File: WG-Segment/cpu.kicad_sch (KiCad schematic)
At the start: 28 parts, among them J201 Conn_01x03, J202 Conn_01x02, J203 Conn_01x04, SW201 SPST-NO, U201 W25Q16JV, U202 RP2040, Y201 12MHz

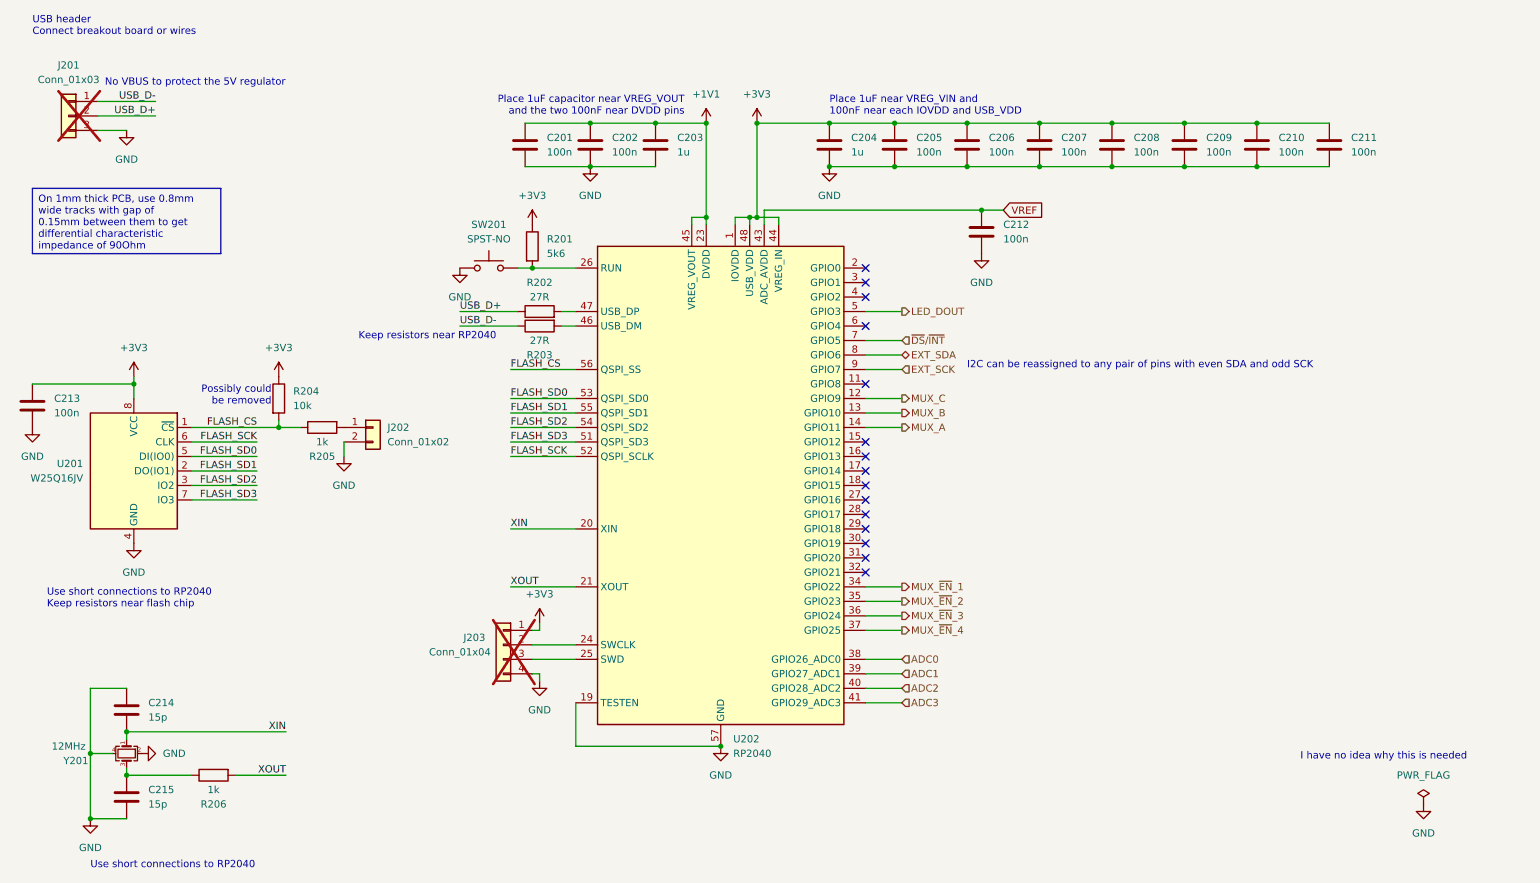
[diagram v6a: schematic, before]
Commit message: Minor pinout adjustments
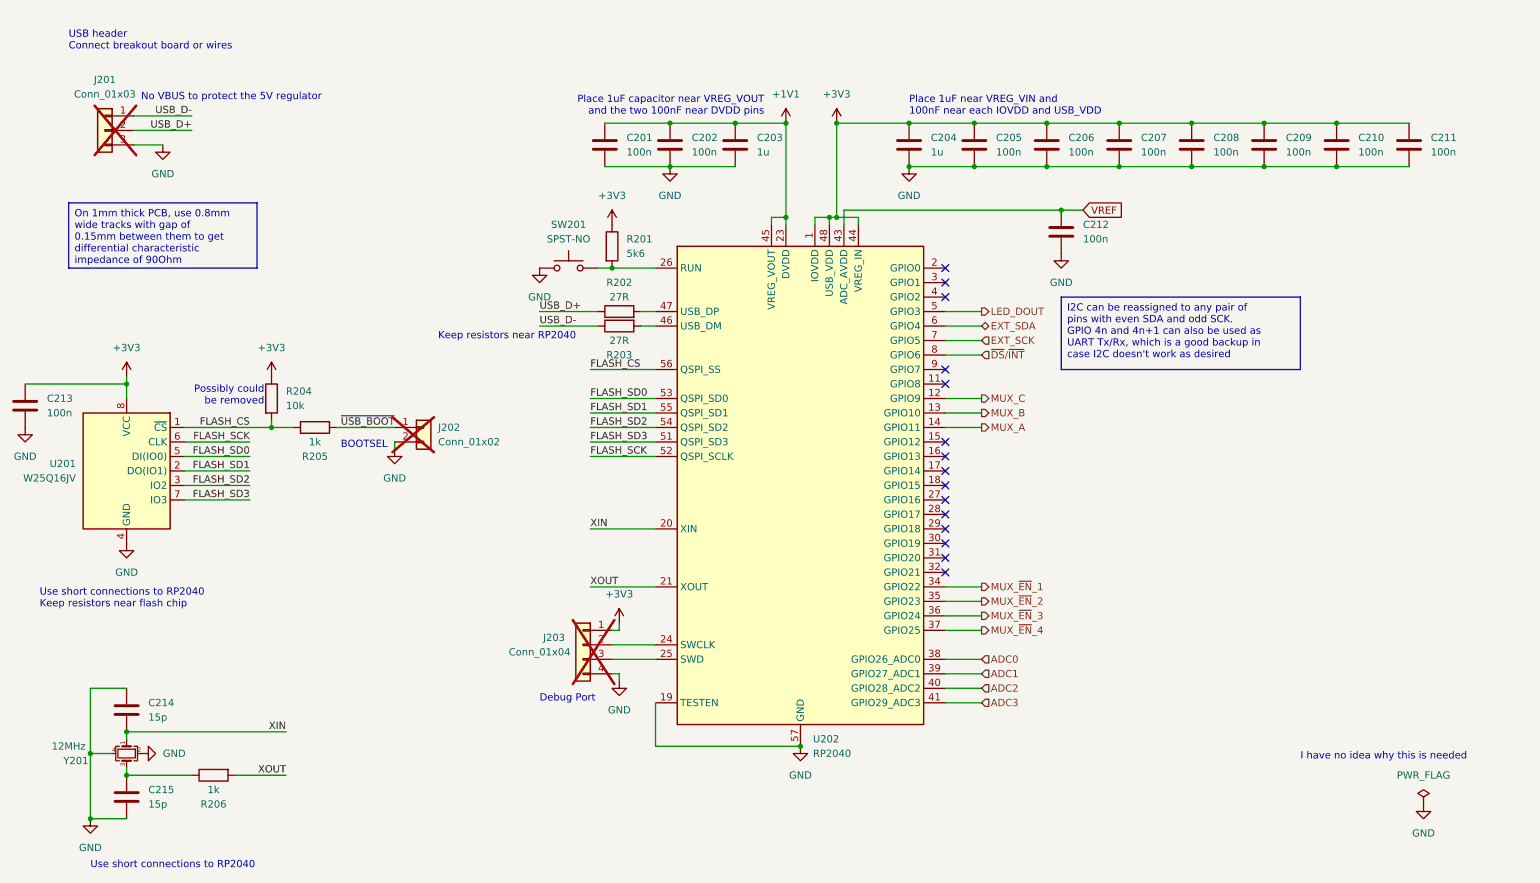
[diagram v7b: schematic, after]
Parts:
- J202: now not fitted; now left out of the parts list
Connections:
- net EXT_SCK: now also U202.7 (GPIO5); no longer U202.9 (GPIO7)
- net EXT_SDA: now also U202.6 (GPIO4); no longer U202.8 (GPIO6)
- net ~{DS}/~{INT}: now also U202.8 (GPIO6); no longer U202.7 (GPIO5)
- net ~{USB_BOOT}: now reaches J202.1 (Pin_1), R205.2
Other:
- note added: "BOOTSEL"
- note added: "Debug Port"
- note removed: "I2C can be reassigned to any pair of pins with even SDA and odd SCK"
- moved on the sheet: C201, C202, C203, C204, C205, C206, C207, C208, C209, C210, C211, C212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

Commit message: Fix build issues
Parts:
- C201, C202, C205, C206, C207, C208, C209, C210, C211, C212, C213: value 100n -> 0.1u; Desc (none) -> CAP CER 0.1uF 10V 0402
- C203, C204: Desc (none) -> CAP CER 1uF 10V 0402
- C214, C215: Desc (none) -> CAP CER 15pF 10V 0402
- R201: Desc (none) -> RES 5k6 1/16W 1% 0402
- R202, R203: Desc (none) -> RES 27R 1/16W 1% 0402
- R204: Desc (none) -> RES 10k 1/16W 1% 0402
- R205, R206: Desc (none) -> RES 1k 1/16W 1% 0402
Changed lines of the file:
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@@
       (effects (font (size 1.27 1.27)) (justify left))
     )
-    (property "Value" "100n" (at 270.51 40.64 0)
+    (property "Value" "0.1u" (at 270.51 40.64 0)
       (effects (font (size 1.27 1.27)) (justify left))
     )
@@
       (effects (font (size 1.27 1.27)) hide)
     )
-    (property "Description" "CAP CER 100nF 10V 0402" (at 266.7 39.37 0)
+    (property "Desc" "CAP CER 0.1uF 10V 0402" (at 266.7 39.37 0)
       (effects (font (size 1.27 1.27)) hide)
     )
@@
       (effects (font (size 1.27 1.27)) hide)
     )
-    (property "Description" "CAP CER 15pF 10V 0402" (at 41.91 138.43 0)
+    (property "Desc" "CAP CER 15pF 10V 0402" (at 41.91 138.43 0)
       (effects (font (size 1.27 1.27)) hide)
     )
@@
       (effects (font (size 1.27 1.27)) hide)
     )
-    (property "Description" "" (at 38.1 36.83 0)
-      (effects (font (size 1.27 1.27)) hide)
-    )
     (pin "1")
     (pin "3")
@@
       (effects (font (size 1.27 1.27)) hide)
     )
-    (property "Description" "" (at 119.38 60.96 0)
-      (effects (font (size 1.27 1.27)) hide)
-    )
     (pin "2")
     (pin "1")
@@
       (effects (font (size 1.27 1.27)) hide)
     )
-    (property "Description" "RES 10k 1/16W 1% 0402" (at 67.31 83.82 0)
+    (property "Desc" "RES 10k 1/16W 1% 0402" (at 67.31 83.82 0)
       (effects (font (size 1.27 1.27)) hide)
     )
@@
       (effects (font (size 1.27 1.27)) hide)
     )
-    (property "Description" "" (at 93.98 88.9 0)
-      (effects (font (size 1.27 1.27)) hide)
-    )
     (pin "2")
     (pin "1")
@@
       (effects (font (size 1.27 1.27)) hide)
     )
-    (property "Description" "RES 27R 1/16W 1% 0402" (at 128.27 71.12 0)
+    (property "Desc" "RES 27R 1/16W 1% 0402" (at 128.27 71.12 0)
       (effects (font (size 1.27 1.27)) hide)
     )
@@
       (effects (font (size 1.27 1.27)) hide)
     )
-    (property "Description" "CAP CER 15pF 10V 0402" (at 41.91 153.67 0)
+    (property "Desc" "CAP CER 15pF 10V 0402" (at 41.91 153.67 0)
       (effects (font (size 1.27 1.27)) hide)
     )
@@
       (effects (font (size 1.27 1.27)) (justify left))
     )
-    (property "Value" "100n" (at 257.81 40.64 0)
+    (property "Value" "0.1u" (at 257.81 40.64 0)
       (effects (font (size 1.27 1.27)) (justify left))
     )
@@
       (effects (font (size 1.27 1.27)) hide)
     )
-    (property "Description" "CAP CER 100nF 10V 0402" (at 254 39.37 0)
+    (property "Desc" "CAP CER 0.1uF 10V 0402" (at 254 39.37 0)
       (effects (font (size 1.27 1.27)) hide)
     )
@@
     )
     (property "Manufacturer" "Winbond Electronics" (at 41.91 96.52 0)
-      (effects (font (size 1.27 1.27)) hide)
-    )
-    (property "Description" "" (at 41.91 96.52 0)
       (effects (font (size 1.27 1.27)) hide)
     )
@@
     )
     (property "Manufacturer" "" (at 121.92 127 0)
-      (effects (font (size 1.27 1.27)) hide)
-    )
-    (property "Description" "" (at 121.92 127 0)
       (effects (font (size 1.27 1.27)) hide)
     )
@@
       (effects (font (size 1.27 1.27)) (justify left))
     )
-    (property "Value" "100n" (at 140.97 40.64 0)
+    (property "Value" "0.1u" (at 140.97 40.64 0)
       (effects (font (size 1.27 1.27)) (justify left))
     )
@@
       (effects (font (size 1.27 1.27)) hide)
     )
-    (property "Description" "CAP CER 100nF 10V 0402" (at 137.16 39.37 0)
+    (property "Desc" "CAP CER 0.1uF 10V 0402" (at 137.16 39.37 0)
       (effects (font (size 1.27 1.27)) hide)
     )
@@
       (effects (font (size 1.27 1.27)) hide)
     )
-    (property "Description" "CAP CER 1uF 10V 0402" (at 179.07 39.37 0)
+    (property "Desc" "CAP CER 1uF 10V 0402" (at 179.07 39.37 0)
       (effects (font (size 1.27 1.27)) hide)
     )
@@
       (effects (font (size 1.27 1.27)) hide)
     )
-    (property "Description" "CAP CER 1uF 10V 0402" (at 148.59 39.37 0)
+    (property "Desc" "CAP CER 1uF 10V 0402" (at 148.59 39.37 0)
       (effects (font (size 1.27 1.27)) hide)
     )
@@
       (effects (font (size 1.27 1.27)) (justify left))
     )
-    (property "Value" "100n" (at 207.01 40.64 0)
+    (property "Value" "0.1u" (at 207.01 40.64 0)
       (effects (font (size 1.27 1.27)) (justify left))
     )
@@
       (effects (font (size 1.27 1.27)) hide)
     )
-    (property "Description" "CAP CER 100nF 10V 0402" (at 203.2 39.37 0)
+    (property "Desc" "CAP CER 0.1uF 10V 0402" (at 203.2 39.37 0)
       (effects (font (size 1.27 1.27)) hide)
     )
@@
       (effects (font (size 1.27 1.27)) (justify left))
     )
-    (property "Value" "100n" (at 209.55 55.88 0)
+    (property "Value" "0.1u" (at 209.55 55.88 0)
       (effects (font (size 1.27 1.27)) (justify left))
     )
@@
       (effects (font (size 1.27 1.27)) hide)
     )
-    (property "Description" "CAP CER 100nF 10V 0402" (at 205.74 54.61 0)
+    (property "Desc" "CAP CER 0.1uF 10V 0402" (at 205.74 54.61 0)
       (effects (font (size 1.27 1.27)) hide)
     )
@@
       (effects (font (size 1.27 1.27)) hide)
     )
-    (property "Description" "RES 1k 1/16W 1% 0402" (at 74.93 88.9 0)
+    (property "Desc" "RES 1k 1/16W 1% 0402" (at 74.93 88.9 0)
       (effects (font (size 1.27 1.27)) hide)
     )
@@
       (effects (font (size 1.27 1.27)) (justify left))
     )
-    (property "Value" "100n" (at 232.41 40.64 0)
+    (property "Value" "0.1u" (at 232.41 40.64 0)
       (effects (font (size 1.27 1.27)) (justify left))
     )
@@
       (effects (font (size 1.27 1.27)) hide)
     )
-    (property "Description" "CAP CER 100nF 10V 0402" (at 228.6 39.37 0)
+    (property "Desc" "CAP CER 0.1uF 10V 0402" (at 228.6 39.37 0)
       (effects (font (size 1.27 1.27)) hide)
     )
@@
       (effects (font (size 1.27 1.27)) (justify left))
     )
-    (property "Value" "100n" (at 245.11 40.64 0)
+    (property "Value" "0.1u" (at 245.11 40.64 0)
       (effects (font (size 1.27 1.27)) (justify left))
     )
@@
       (effects (font (size 1.27 1.27)) hide)
     )
-    (property "Description" "CAP CER 100nF 10V 0402" (at 241.3 39.37 0)
+    (property "Desc" "CAP CER 0.1uF 10V 0402" (at 241.3 39.37 0)
       (effects (font (size 1.27 1.27)) hide)
     )
@@
       (effects (font (size 1.27 1.27)) (justify left))
     )
-    (property "Value" "100n" (at 27.94 86.36 0)
+    (property "Value" "0.1u" (at 27.94 86.36 0)
       (effects (font (size 1.27 1.27)) (justify left))
     )
@@
       (effects (font (size 1.27 1.27)) hide)
     )
-    (property "Description" "CAP CER 100nF 10V 0402" (at 24.13 85.09 0)
+    (property "Desc" "CAP CER 0.1uF 10V 0402" (at 24.13 85.09 0)
       (effects (font (size 1.27 1.27)) hide)
     )
@@
       (effects (font (size 1.27 1.27)) hide)
     )
-    (property "Description" "" (at 41.91 146.05 0)
-      (effects (font (size 1.27 1.27)) hide)
-    )
     (pin "2")
     (pin "1")
@@
       (effects (font (size 1.27 1.27)) hide)
     )
-    (property "Description" "RES 27R 1/16W 1% 0402" (at 128.27 68.58 0)
+    (property "Desc" "RES 27R 1/16W 1% 0402" (at 128.27 68.58 0)
       (effects (font (size 1.27 1.27)) hide)
     )
@@
       (effects (font (size 1.27 1.27)) hide)
     )
-    (property "Description" "RES 5k6 1/16W 1% 0402" (at 127 57.15 0)
+    (property "Desc" "RES 5k6 1/16W 1% 0402" (at 127 57.15 0)
       (effects (font (size 1.27 1.27)) hide)
     )
@@
       (effects (font (size 1.27 1.27)) (justify left))
     )
-    (property "Value" "100n" (at 194.31 40.64 0)
+    (property "Value" "0.1u" (at 194.31 40.64 0)
       (effects (font (size 1.27 1.27)) (justify left))
     )
@@
       (effects (font (size 1.27 1.27)) hide)
     )
-    (property "Description" "CAP CER 100nF 10V 0402" (at 190.5 39.37 0)
+    (property "Desc" "CAP CER 0.1uF 10V 0402" (at 190.5 39.37 0)
       (effects (font (size 1.27 1.27)) hide)
     )
@@
       (effects (font (size 1.27 1.27)) hide)
     )
-    (property "Description" "RES 1k 1/16W 1% 0402" (at 57.15 149.86 0)
+    (property "Desc" "RES 1k 1/16W 1% 0402" (at 57.15 149.86 0)
       (effects (font (size 1.27 1.27)) hide)
     )
@@
       (effects (font (size 1.27 1.27)) (justify left))
     )
-    (property "Value" "100n" (at 219.71 40.64 0)
+    (property "Value" "0.1u" (at 219.71 40.64 0)
       (effects (font (size 1.27 1.27)) (justify left))
     )
@@
       (effects (font (size 1.27 1.27)) hide)
     )
-    (property "Description" "CAP CER 100nF 10V 0402" (at 215.9 39.37 0)
+    (property "Desc" "CAP CER 0.1uF 10V 0402" (at 215.9 39.37 0)
       (effects (font (size 1.27 1.27)) hide)
     )
@@
       (effects (font (size 1.27 1.27)) (justify left))
     )
-    (property "Value" "100n" (at 129.54 40.64 0)
+    (property "Value" "0.1u" (at 129.54 40.64 0)
       (effects (font (size 1.27 1.27)) (justify left))
     )
@@
       (effects (font (size 1.27 1.27)) hide)
     )
-    (property "Description" "CAP CER 100nF 10V 0402" (at 125.73 39.37 0)
-      (effects (font (size 1.27 1.27)) hide)
-    )
+    (property "Desc" "CAP CER 0.1uF 10V 0402" (at 125.73 39.37 0)
+      (effects (font (size 1.27 1.27)) hide)
+    )
